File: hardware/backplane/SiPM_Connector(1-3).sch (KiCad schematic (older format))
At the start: 8 parts, among them J101 Conn_02x34_Odd_Even, J102 ERF8-060-05.0-L-DV, J103 Conn_02x34_Odd_Even, J201 Conn_02x34_Odd_Even-Connector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, J203 Conn_02x34_Odd_Even-Connector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, J301 Conn_02x34_Odd_Even-Connector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, J302 ERF8-060-05.0-L-DV, J303 Conn_02x34_Odd_Even-Connector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

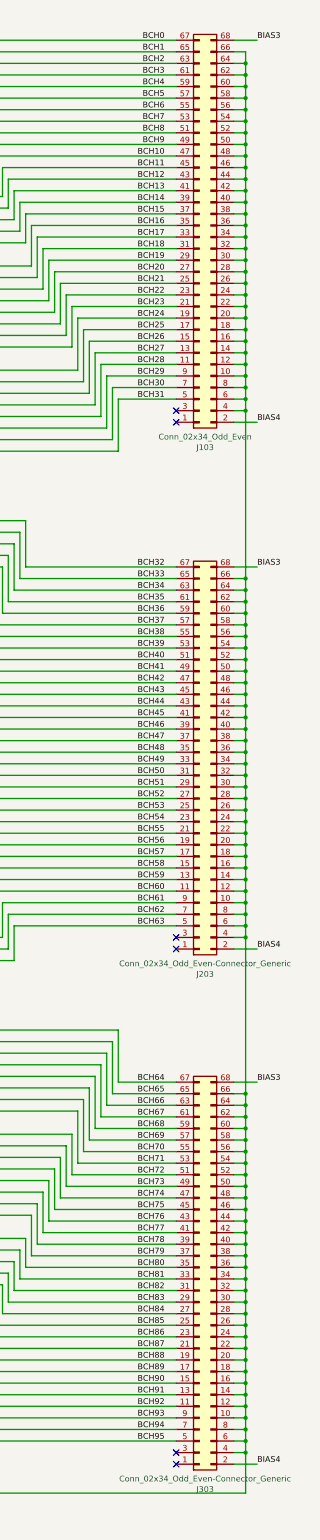
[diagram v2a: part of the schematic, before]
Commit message: SiPM Board RevC layout modified
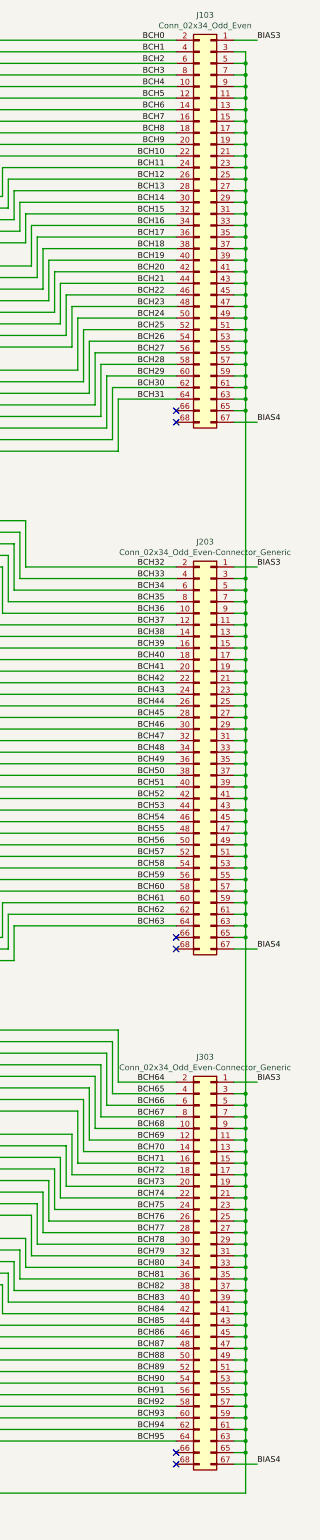
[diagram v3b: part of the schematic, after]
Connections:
- net BCH0: now also J103.2 (Pin_2); no longer J103.67 (Pin_67)
- net BCH1: now also J103.4 (Pin_4); no longer J103.65 (Pin_65)
- net BCH10: now also J103.22 (Pin_22); no longer J103.47 (Pin_47)
- net BCH11: now also J103.24 (Pin_24); no longer J103.45 (Pin_45)
- net BCH12: now also J103.26 (Pin_26); no longer J103.43 (Pin_43)
- net BCH13: now also J103.28 (Pin_28); no longer J103.41 (Pin_41)
- net BCH14: now also J103.30 (Pin_30); no longer J103.39 (Pin_39)
- net BCH15: now also J103.32 (Pin_32); no longer J103.37 (Pin_37)
- net BCH16: now also J103.34 (Pin_34); no longer J103.35 (Pin_35)
- net BCH17: now also J103.36 (Pin_36); no longer J103.33 (Pin_33)
- net BCH18: now also J103.38 (Pin_38); no longer J103.31 (Pin_31)
- net BCH19: now also J103.40 (Pin_40); no longer J103.29 (Pin_29)
- net BCH2: now also J103.6 (Pin_6); no longer J103.63 (Pin_63)
- net BCH20: now also J103.42 (Pin_42); no longer J103.27 (Pin_27)
- net BCH21: now also J103.44 (Pin_44); no longer J103.25 (Pin_25)
- net BCH22: now also J103.46 (Pin_46); no longer J103.23 (Pin_23)
- net BCH23: now also J103.48 (Pin_48); no longer J103.21 (Pin_21)
- net BCH24: now also J103.50 (Pin_50); no longer J103.19 (Pin_19)
- net BCH25: now also J103.52 (Pin_52); no longer J103.17 (Pin_17)
- net BCH26: now also J103.54 (Pin_54); no longer J103.15 (Pin_15)
- net BCH27: now also J103.56 (Pin_56); no longer J103.13 (Pin_13)
- net BCH28: now also J103.58 (Pin_58); no longer J103.11 (Pin_11)
- net BCH29: now also J103.60 (Pin_60); no longer J103.9 (Pin_9)
- net BCH3: now also J103.8 (Pin_8); no longer J103.61 (Pin_61)
- net BCH30: now also J103.62 (Pin_62); no longer J103.7 (Pin_7)
- net BCH31: now also J103.64 (Pin_64); no longer J103.5 (Pin_5)
- net BCH32: now also J203.2 (Pin_2); no longer J203.67 (Pin_67)
- net BCH33: now also J203.4 (Pin_4); no longer J203.65 (Pin_65)
- net BCH34: now also J203.6 (Pin_6); no longer J203.63 (Pin_63)
- net BCH35: now also J203.8 (Pin_8); no longer J203.61 (Pin_61)
- net BCH36: now also J203.10 (Pin_10); no longer J203.59 (Pin_59)
- net BCH37: now also J203.12 (Pin_12); no longer J203.57 (Pin_57)
- net BCH38: now also J203.14 (Pin_14); no longer J203.55 (Pin_55)
- net BCH39: now also J203.16 (Pin_16); no longer J203.53 (Pin_53)
- net BCH4: now also J103.10 (Pin_10); no longer J103.59 (Pin_59)
- net BCH40: now also J203.18 (Pin_18); no longer J203.51 (Pin_51)
- net BCH41: now also J203.20 (Pin_20); no longer J203.49 (Pin_49)
- net BCH42: now also J203.22 (Pin_22); no longer J203.47 (Pin_47)
- net BCH43: now also J203.24 (Pin_24); no longer J203.45 (Pin_45)
- net BCH44: now also J203.26 (Pin_26); no longer J203.43 (Pin_43)
- net BCH45: now also J203.28 (Pin_28); no longer J203.41 (Pin_41)
- net BCH46: now also J203.30 (Pin_30); no longer J203.39 (Pin_39)
- net BCH47: now also J203.32 (Pin_32); no longer J203.37 (Pin_37)
- net BCH48: now also J203.34 (Pin_34); no longer J203.35 (Pin_35)
- net BCH49: now also J203.36 (Pin_36); no longer J203.33 (Pin_33)
- net BCH5: now also J103.12 (Pin_12); no longer J103.57 (Pin_57)
- net BCH50: now also J203.38 (Pin_38); no longer J203.31 (Pin_31)
- net BCH51: now also J203.40 (Pin_40); no longer J203.29 (Pin_29)
- net BCH52: now also J203.42 (Pin_42); no longer J203.27 (Pin_27)
- net BCH53: now also J203.44 (Pin_44); no longer J203.25 (Pin_25)
- net BCH54: now also J203.46 (Pin_46); no longer J203.23 (Pin_23)
- net BCH55: now also J203.48 (Pin_48); no longer J203.21 (Pin_21)
- net BCH56: now also J203.50 (Pin_50); no longer J203.19 (Pin_19)
- net BCH57: now also J203.52 (Pin_52); no longer J203.17 (Pin_17)
- net BCH58: now also J203.54 (Pin_54); no longer J203.15 (Pin_15)
- net BCH59: now also J203.56 (Pin_56); no longer J203.13 (Pin_13)
- net BCH6: now also J103.14 (Pin_14); no longer J103.55 (Pin_55)
- net BCH60: now also J203.58 (Pin_58); no longer J203.11 (Pin_11)
- net BCH61: now also J203.60 (Pin_60); no longer J203.9 (Pin_9)
- net BCH62: now also J203.62 (Pin_62); no longer J203.7 (Pin_7)
- net BCH63: now also J203.64 (Pin_64); no longer J203.5 (Pin_5)
- net BCH64: now also J303.2 (Pin_2); no longer J303.67 (Pin_67)
- net BCH65: now also J303.4 (Pin_4); no longer J303.65 (Pin_65)
- net BCH66: now also J303.6 (Pin_6); no longer J303.63 (Pin_63)
- net BCH67: now also J303.8 (Pin_8); no longer J303.61 (Pin_61)
- net BCH68: now also J303.10 (Pin_10); no longer J303.59 (Pin_59)
- net BCH69: now also J303.12 (Pin_12); no longer J303.57 (Pin_57)
- net BCH7: now also J103.16 (Pin_16); no longer J103.53 (Pin_53)
- net BCH70: now also J303.14 (Pin_14); no longer J303.55 (Pin_55)
- net BCH71: now also J303.16 (Pin_16); no longer J303.53 (Pin_53)
- net BCH72: now also J303.18 (Pin_18); no longer J303.51 (Pin_51)
- net BCH73: now also J303.20 (Pin_20); no longer J303.49 (Pin_49)
- net BCH74: now also J303.22 (Pin_22); no longer J303.47 (Pin_47)
- net BCH75: now also J303.24 (Pin_24); no longer J303.45 (Pin_45)
- net BCH76: now also J303.26 (Pin_26); no longer J303.43 (Pin_43)
- net BCH77: now also J303.28 (Pin_28); no longer J303.41 (Pin_41)
- net BCH78: now also J303.30 (Pin_30); no longer J303.39 (Pin_39)
- net BCH79: now also J303.32 (Pin_32); no longer J303.37 (Pin_37)
- net BCH8: now also J103.18 (Pin_18); no longer J103.51 (Pin_51)
- net BCH80: now also J303.34 (Pin_34); no longer J303.35 (Pin_35)
- net BCH81: now also J303.36 (Pin_36); no longer J303.33 (Pin_33)
- net BCH82: now also J303.38 (Pin_38); no longer J303.31 (Pin_31)
- net BCH83: now also J303.40 (Pin_40); no longer J303.29 (Pin_29)
- net BCH84: now also J303.42 (Pin_42); no longer J303.27 (Pin_27)
- net BCH85: now also J303.44 (Pin_44); no longer J303.25 (Pin_25)
- net BCH86: now also J303.46 (Pin_46); no longer J303.23 (Pin_23)
- net BCH87: now also J303.48 (Pin_48); no longer J303.21 (Pin_21)
- net BCH88: now also J303.50 (Pin_50); no longer J303.19 (Pin_19)
- net BCH89: now also J303.52 (Pin_52); no longer J303.17 (Pin_17)
- net BCH9: now also J103.20 (Pin_20); no longer J103.49 (Pin_49)
- net BCH90: now also J303.54 (Pin_54); no longer J303.15 (Pin_15)
- net BCH91: now also J303.56 (Pin_56); no longer J303.13 (Pin_13)
- net BCH92: now also J303.58 (Pin_58); no longer J303.11 (Pin_11)
- net BCH93: now also J303.60 (Pin_60); no longer J303.9 (Pin_9)
- net BCH94: now also J303.62 (Pin_62); no longer J303.7 (Pin_7)
- net BCH95: now also J303.64 (Pin_64); no longer J303.5 (Pin_5)
- net BIAS3: now also J103.1 (Pin_1), J203.1 (Pin_1), J303.1 (Pin_1); no longer J103.68 (Pin_68), J203.68 (Pin_68), J303.68 (Pin_68)
- net BIAS4: now also J103.67 (Pin_67), J203.67 (Pin_67), J303.67 (Pin_67); no longer J103.2 (Pin_2), J203.2 (Pin_2), J303.2 (Pin_2)
- net GND: now also J103.11 (Pin_11), J103.13 (Pin_13), J103.15 (Pin_15), J103.17 (Pin_17), J103.19 (Pin_19), J103.21 (Pin_21), J103.23 (Pin_23), J103.25 (Pin_25), J103.27 (Pin_27), J103.29 (Pin_29), J103.3 (Pin_3), J103.31 (Pin_31), J103.33 (Pin_33), J103.35 (Pin_35), J103.37 (Pin_37), J103.39 (Pin_39), J103.41 (Pin_41), J103.43 (Pin_43), J103.45 (Pin_45), J103.47 (Pin_47), J103.49 (Pin_49), J103.5 (Pin_5), J103.51 (Pin_51), J103.53 (Pin_53), J103.55 (Pin_55), J103.57 (Pin_57), J103.59 (Pin_59), J103.61 (Pin_61), J103.63 (Pin_63), J103.65 (Pin_65), J103.7 (Pin_7), J103.9 (Pin_9), J203.11 (Pin_11), J203.13 (Pin_13), J203.15 (Pin_15), J203.17 (Pin_17), J203.19 (Pin_19), J203.21 (Pin_21), J203.23 (Pin_23), J203.25 (Pin_25), J203.27 (Pin_27), J203.29 (Pin_29), J203.3 (Pin_3), J203.31 (Pin_31), J203.33 (Pin_33), J203.35 (Pin_35), J203.37 (Pin_37), J203.39 (Pin_39), J203.41 (Pin_41), J203.43 (Pin_43), J203.45 (Pin_45), J203.47 (Pin_47), J203.49 (Pin_49), J203.5 (Pin_5), J203.51 (Pin_51), J203.53 (Pin_53), J203.55 (Pin_55), J203.57 (Pin_57), J203.59 (Pin_59), J203.61 (Pin_61), J203.63 (Pin_63), J203.65 (Pin_65), J203.7 (Pin_7), J203.9 (Pin_9), J303.11 (Pin_11), J303.13 (Pin_13), J303.15 (Pin_15), J303.17 (Pin_17), J303.19 (Pin_19), J303.21 (Pin_21), J303.23 (Pin_23), J303.25 (Pin_25), J303.27 (Pin_27), J303.29 (Pin_29), J303.3 (Pin_3), J303.31 (Pin_31), J303.33 (Pin_33), J303.35 (Pin_35), J303.37 (Pin_37), J303.39 (Pin_39), J303.41 (Pin_41), J303.43 (Pin_43), J303.45 (Pin_45), J303.47 (Pin_47), J303.49 (Pin_49), J303.5 (Pin_5), J303.51 (Pin_51), J303.53 (Pin_53), J303.55 (Pin_55), J303.57 (Pin_57), J303.59 (Pin_59), J303.61 (Pin_61), J303.63 (Pin_63), J303.65 (Pin_65), J303.7 (Pin_7), J303.9 (Pin_9); no longer J103.10 (Pin_10), J103.12 (Pin_12), J103.14 (Pin_14), J103.16 (Pin_16), J103.18 (Pin_18), J103.20 (Pin_20), J103.22 (Pin_22), J103.24 (Pin_24), J103.26 (Pin_26), J103.28 (Pin_28), J103.30 (Pin_30), J103.32 (Pin_32), J103.34 (Pin_34), J103.36 (Pin_36), J103.38 (Pin_38), J103.4 (Pin_4), J103.40 (Pin_40), J103.42 (Pin_42), J103.44 (Pin_44), J103.46 (Pin_46), J103.48 (Pin_48), J103.50 (Pin_50), J103.52 (Pin_52), J103.54 (Pin_54), J103.56 (Pin_56), J103.58 (Pin_58), J103.6 (Pin_6), J103.60 (Pin_60), J103.62 (Pin_62), J103.64 (Pin_64), J103.66 (Pin_66), J103.8 (Pin_8), J203.10 (Pin_10), J203.12 (Pin_12), J203.14 (Pin_14), J203.16 (Pin_16), J203.18 (Pin_18), J203.20 (Pin_20), J203.22 (Pin_22), J203.24 (Pin_24), J203.26 (Pin_26), J203.28 (Pin_28), J203.30 (Pin_30), J203.32 (Pin_32), J203.34 (Pin_34), J203.36 (Pin_36), J203.38 (Pin_38), J203.4 (Pin_4), J203.40 (Pin_40), J203.42 (Pin_42), J203.44 (Pin_44), J203.46 (Pin_46), J203.48 (Pin_48), J203.50 (Pin_50), J203.52 (Pin_52), J203.54 (Pin_54), J203.56 (Pin_56), J203.58 (Pin_58), J203.6 (Pin_6), J203.60 (Pin_60), J203.62 (Pin_62), J203.64 (Pin_64), J203.66 (Pin_66), J203.8 (Pin_8), J303.10 (Pin_10), J303.12 (Pin_12), J303.14 (Pin_14), J303.16 (Pin_16), J303.18 (Pin_18), J303.20 (Pin_20), J303.22 (Pin_22), J303.24 (Pin_24), J303.26 (Pin_26), J303.28 (Pin_28), J303.30 (Pin_30), J303.32 (Pin_32), J303.34 (Pin_34), J303.36 (Pin_36), J303.38 (Pin_38), J303.4 (Pin_4), J303.40 (Pin_40), J303.42 (Pin_42), J303.44 (Pin_44), J303.46 (Pin_46), J303.48 (Pin_48), J303.50 (Pin_50), J303.52 (Pin_52), J303.54 (Pin_54), J303.56 (Pin_56), J303.58 (Pin_58), J303.6 (Pin_6), J303.60 (Pin_60), J303.62 (Pin_62), J303.64 (Pin_64), J303.66 (Pin_66), J303.8 (Pin_8)
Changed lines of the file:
@@
 Wire Wire Line
 	4300 3350 5000 3350
-$Comp
-L backplane-rescue:ERF8-060-XX.X-X-DV-ERF8-060-05.0-L-DV-backplane-prototype-rescue J102
-U 1 1 63C5DEAC
-P 6000 2350
-F 0 "J102" H 6500 2617 50  0000 C CNN
-F 1 "ERF8-060-05.0-L-DV" H 6500 2526 50  0000 C CNN
-F 2 "backplane:ERF8-060-05.0-L-DV" H 6000 2350 50  0001 L BNN
-F 3 "https://suddendocs.samtec.com/productspecs/erm8-erf8.pdf" H 6000 2350 50  0001 L BNN
-F 4 "ERF8-060-05.0-L-DV-L-K-TR" H 6000 2350 50  0001 C CNN "MFN"
-F 5 "Mouser Electronics" H 6000 2350 50  0001 C CNN "Supplier"
-F 6 "200-ERF806005.0LDVLK" H 6000 2350 50  0001 C CNN "Supplier P/N"
-F 7 "$9.61" H 6000 2350 50  0001 C CNN "Item Cost"
-	1    6000 2350
-	-1   0    0    -1
-$EndComp
 Wire Wire Line
 	4000 3950 5000 3950
@@
 L backplane-rescue:Conn_02x34_Odd_Even-Connector_Generic-backplane-prototype-rescue J103
 U 1 1 63C5DEAA
-P 8550 4000
+P 8650 3900
 AR Path="/63C5DEAA" Ref="J103"  Part="1"
 AR Path="/60955FE3/63C5DEAA" Ref="J103"  Part="1"
-F 0 "J103" H 8600 5817 50  0000 C CNN
-F 1 "Conn_02x34_Odd_Even" H 8600 5726 50  0000 C CNN
-F 2 "backplane:SAMTEC_CLM-134-02-F-D" H 8550 4000 50  0001 C CNN
-F 3 "http://suddendocs.samtec.com/catalog_english/clm_sm.pdf" H 8550 4000 50  0001 C CNN
-F 4 "CLM-134-02-F-D" H 8550 4000 50  0001 C CNN "MFN"
-F 5 "Digi-Key" H 8550 4000 50  0001 C CNN "Supplier"
-F 6 "CLM-134-02-F-D-ND" H 8550 4000 50  0001 C CNN "Supplier P/N"
-F 7 "$9.02" H 8550 4000 50  0001 C CNN "Item Cost"
-	1    8550 4000
-	1    0    0    1
+F 0 "J103" H 8700 5717 50  0000 C CNN
+F 1 "Conn_02x34_Odd_Even" H 8700 5626 50  0000 C CNN
+F 2 "backplane:SAMTEC_CLM-134-02-F-D" H 8650 3900 50  0001 C CNN
+F 3 "http://suddendocs.samtec.com/catalog_english/clm_sm.pdf" H 8650 3900 50  0001 C CNN
+F 4 "CLM-134-02-F-D" H 8650 3900 50  0001 C CNN "MFN"
+F 5 "Digi-Key" H 8650 3900 50  0001 C CNN "Supplier"
+F 6 "CLM-134-02-F-D-ND" H 8650 3900 50  0001 C CNN "Supplier P/N"
+F 7 "$9.02" H 8650 3900 50  0001 C CNN "Item Cost"
+	1    8650 3900
+	-1   0    0    -1
 $EndComp
 $Comp
@@
 L backplane-rescue:Conn_02x34_Odd_Even-Connector_Generic-backplane-prototype-rescue J303
 U 1 1 6818B91B
-P 8550 13000
+P 8650 12900
 AR Path="/6818B91B" Ref="J303"  Part="1"
 AR Path="/60955FE3/6818B91B" Ref="J303"  Part="1"
-F 0 "J303" H 8600 14817 50  0000 C CNN
-F 1 "Conn_02x34_Odd_Even-Connector_Generic" H 8600 14726 50  0000 C CNN
-F 2 "backplane:SAMTEC_CLM-134-02-F-D" H 8550 13000 50  0001 C CNN
-F 3 "" H 8550 13000 50  0001 C CNN
-	1    8550 13000
-	1    0    0    1
+F 0 "J303" H 8700 14717 50  0000 C CNN
+F 1 "Conn_02x34_Odd_Even-Connector_Generic" H 8700 14626 50  0000 C CNN
+F 2 "backplane:SAMTEC_CLM-134-02-F-D" H 8650 12900 50  0001 C CNN
+F 3 "" H 8650 12900 50  0001 C CNN
+	1    8650 12900
+	-1   0    0    -1
 $EndComp
 $Comp
@@
 L backplane-rescue:Conn_02x34_Odd_Even-Connector_Generic-backplane-prototype-rescue J203
 U 1 1 6818B914
-P 8550 8550
+P 8650 8450
 AR Path="/6818B914" Ref="J203"  Part="1"
 AR Path="/60955FE3/6818B914" Ref="J203"  Part="1"
-F 0 "J203" H 8600 10367 50  0000 C CNN
-F 1 "Conn_02x34_Odd_Even-Connector_Generic" H 8600 10276 50  0000 C CNN
-F 2 "backplane:SAMTEC_CLM-134-02-F-D" H 8550 8550 50  0001 C CNN
-F 3 "" H 8550 8550 50  0001 C CNN
-	1    8550 8550
-	1    0    0    1
+F 0 "J203" H 8700 10267 50  0000 C CNN
+F 1 "Conn_02x34_Odd_Even-Connector_Generic" H 8700 10176 50  0000 C CNN
+F 2 "backplane:SAMTEC_CLM-134-02-F-D" H 8650 8450 50  0001 C CNN
+F 3 "" H 8650 8450 50  0001 C CNN
+	1    8650 8450
+	-1   0    0    -1
 $EndComp
 NoConn ~ 8350 10150
@@
 Text Label 2750 11300 0    50   ~ 0
 CH64
+$Comp
+L backplane-rescue:ERF8-060-XX.X-X-DV-ERF8-060-05.0-L-DV-backplane-prototype-rescue J102
+U 1 1 63C5DEAC
+P 6000 2350
+F 0 "J102" H 6500 2617 50  0000 C CNN
+F 1 "ERF8-060-05.0-L-DV" H 6500 2526 50  0000 C CNN
+F 2 "backplane:ERF8-060-05.0-L-DV" H 6000 2350 50  0001 L BNN
+F 3 "https://suddendocs.samtec.com/productspecs/erm8-erf8.pdf" H 6000 2350 50  0001 L BNN
+F 4 "ERF8-060-05.0-L-DV-L-K-TR" H 6000 2350 50  0001 C CNN "MFN"
+F 5 "Mouser Electronics" H 6000 2350 50  0001 C CNN "Supplier"
+F 6 "200-ERF806005.0LDVLK" H 6000 2350 50  0001 C CNN "Supplier P/N"
+F 7 "$9.61" H 6000 2350 50  0001 C CNN "Item Cost"
+	1    6000 2350
+	-1   0    0    -1
+$EndComp
 $EndSCHEMATC

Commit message: Edited Backplane
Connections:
- net BIAS1: no longer J201.2 (Pin_2), J301.2 (Pin_2), J302.116, J302.36
- net BIAS2: no longer J201.68 (Pin_68), J301.68 (Pin_68), J302.120, J302.40
- net BIAS3: no longer J203.1 (Pin_1), J302.115, J302.35, J303.1 (Pin_1)
- net BIAS4: no longer J203.67 (Pin_67), J302.119, J302.39, J303.67 (Pin_67)
- new net BIAS10: J301.68 (Pin_68), J302.120
- new net BIAS11: J302.115, J303.1 (Pin_1)
- new net BIAS12: J302.119, J303.67 (Pin_67)
- new net BIAS5: J201.2 (Pin_2), J302.36
- new net BIAS6: J201.68 (Pin_68), J302.40
- new net BIAS7: J203.1 (Pin_1), J302.35
- new net BIAS8: J203.67 (Pin_67), J302.39
- new net BIAS9: J301.2 (Pin_2), J302.116
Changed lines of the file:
@@
 	6000 10650 6200 10650
 Text Label 6200 10450 0    50   ~ 0
-BIAS3
+BIAS7
 Text Label 6200 10550 0    50   ~ 0
 OUT
 Text Label 6200 10650 0    50   ~ 0
-BIAS4
+BIAS8
 Wire Wire Line
 	6000 14450 6200 14450
@@
 	6000 14650 6200 14650
 Text Label 6200 14450 0    50   ~ 0
-BIAS3
+BIAS11
 Text Label 6200 14550 0    50   ~ 0
 OUT
 Text Label 6200 14650 0    50   ~ 0
-BIAS4
+BIAS12
 Wire Wire Line
 	5000 10450 4800 10450
@@
 	5000 10650 4800 10650
 Text Label 4800 10450 2    50   ~ 0
-BIAS1
+BIAS5
 Text Label 4800 10550 2    50   ~ 0
 VDD
 Text Label 4800 10650 2    50   ~ 0
-BIAS2
+BIAS6
 Wire Wire Line
 	5000 14450 4800 14450
@@
 	5000 14650 4800 14650
 Text Label 4800 14450 2    50   ~ 0
-BIAS1
+BIAS9
 Text Label 4800 14550 2    50   ~ 0
 VDD
 Text Label 4800 14650 2    50   ~ 0
-BIAS2
+BIAS10
 Wire Wire Line
 	4750 8250 5000 8250
@@
 Connection ~ 8950 10050
 Text Label 9050 6850 0    50   ~ 0
-BIAS3
+BIAS7
 Wire Wire Line
 	8850 6850 9050 6850
@@
 Connection ~ 8950 14500
 Text Label 9050 11300 0    50   ~ 0
-BIAS3
+BIAS11
 Wire Wire Line
 	8850 11300 9050 11300
 Text Label 9050 10150 0    50   ~ 0
-BIAS4
+BIAS8
 NoConn ~ 8350 10050
 NoConn ~ 8350 14500
@@
 	2150 14600 1950 14600
 Text Label 1950 14600 2    50   ~ 0
-BIAS2
+BIAS10
 Connection ~ 2050 14500
 Wire Wire Line
 	2150 11300 1950 11300
 Text Label 1950 11300 2    50   ~ 0
-BIAS1
+BIAS9
 Connection ~ 2050 10050
 Wire Wire Line
 	2150 10150 1950 10150
 Text Label 1950 10150 2    50   ~ 0
-BIAS2
+BIAS6
 Text Label 1950 5600 2    50   ~ 0
 BIAS2
@@
 	2150 6850 1950 6850
 Text Label 1950 6850 2    50   ~ 0
-BIAS1
+BIAS5
 Text Label 2750 14500 0    50   ~ 0
 VDD
@@
 	9050 14600 8850 14600
 Text Label 9050 14600 0    50   ~ 0
-BIAS4
+BIAS12
 NoConn ~ 8350 14600
 Wire Wire Line

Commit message: -
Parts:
- J101, J103, J201, J203, J301, J303: symbol backplane-rescue:Conn_02x34_Odd_Even-Connector_Generic-backplane-prototype-rescue -> Connector_Generic:Conn_02x34_Odd_Even
- J102, J302: symbol backplane-rescue:ERF8-060-XX.X-X-DV-ERF8-060-05.0-L-DV-backplane-prototype-rescue -> ERF8-060-05.0-L-DV:ERF8-060-05.0-L-DV
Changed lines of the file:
@@
 	8850 2300 9050 2300
 $Comp
-L backplane-rescue:Conn_02x34_Odd_Even-Connector_Generic-backplane-prototype-rescue J103
+L Connector_Generic:Conn_02x34_Odd_Even J103
 U 1 1 63C5DEAA
 P 8650 3900
@@
 $EndComp
 $Comp
-L backplane-rescue:Conn_02x34_Odd_Even-Connector_Generic-backplane-prototype-rescue J101
+L Connector_Generic:Conn_02x34_Odd_Even J101
 U 1 1 63C5DEA8
 P 2450 3900
@@
 Connection ~ 6100 5950
 $Comp
-L backplane-rescue:GND-power-backplane-prototype-rescue #PWR0102
+L power:GND #PWR0102
 U 1 1 63C5DEAE
 P 5500 14950
@@
 	6100 8150 6100 9450
 $Comp
-L backplane-rescue:ERF8-060-XX.X-X-DV-ERF8-060-05.0-L-DV-backplane-prototype-rescue J302
+L ERF8-060-05.0-L-DV:ERF8-060-05.0-L-DV J302
 U 1 1 63C5DEA7
 P 6000 8750
+AR Path="/63C5DEA7" Ref="J302"  Part="1"
+AR Path="/60955FE3/63C5DEA7" Ref="J302"  Part="1"
 F 0 "J302" H 6500 9017 50  0000 C CNN
 F 1 "ERF8-060-05.0-L-DV" H 6500 8926 50  0000 C CNN
@@
 $EndComp
 $Comp
-L backplane-rescue:Conn_02x34_Odd_Even-Connector_Generic-backplane-prototype-rescue J301
+L Connector_Generic:Conn_02x34_Odd_Even J301
 U 1 1 63C5DEAF
 P 2450 12900
@@
 $EndComp
 $Comp
-L backplane-rescue:Conn_02x34_Odd_Even-Connector_Generic-backplane-prototype-rescue J303
+L Connector_Generic:Conn_02x34_Odd_Even J303
 U 1 1 6818B91B
 P 8650 12900
@@
 $EndComp
 $Comp
-L backplane-rescue:Conn_02x34_Odd_Even-Connector_Generic-backplane-prototype-rescue J201
+L Connector_Generic:Conn_02x34_Odd_Even J201
 U 1 1 6818B913
 P 2450 8450
@@
 	8350 8250 6350 8250
 $Comp
-L backplane-rescue:Conn_02x34_Odd_Even-Connector_Generic-backplane-prototype-rescue J203
+L Connector_Generic:Conn_02x34_Odd_Even J203
 U 1 1 6818B914
 P 8650 8450
@@
 CH64
 $Comp
-L backplane-rescue:ERF8-060-XX.X-X-DV-ERF8-060-05.0-L-DV-backplane-prototype-rescue J102
+L ERF8-060-05.0-L-DV:ERF8-060-05.0-L-DV J102
 U 1 1 63C5DEAC
 P 6000 2350
+AR Path="/63C5DEAC" Ref="J102"  Part="1"
+AR Path="/60955FE3/63C5DEAC" Ref="J102"  Part="1"
 F 0 "J102" H 6500 2617 50  0000 C CNN
 F 1 "ERF8-060-05.0-L-DV" H 6500 2526 50  0000 C CNN
